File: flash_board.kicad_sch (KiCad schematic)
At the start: 9 parts, among them J1 Conn_02x16_Row_Letter_First, J2 Conn_02x03_Counter_Clockwise, U1 SST39SF040

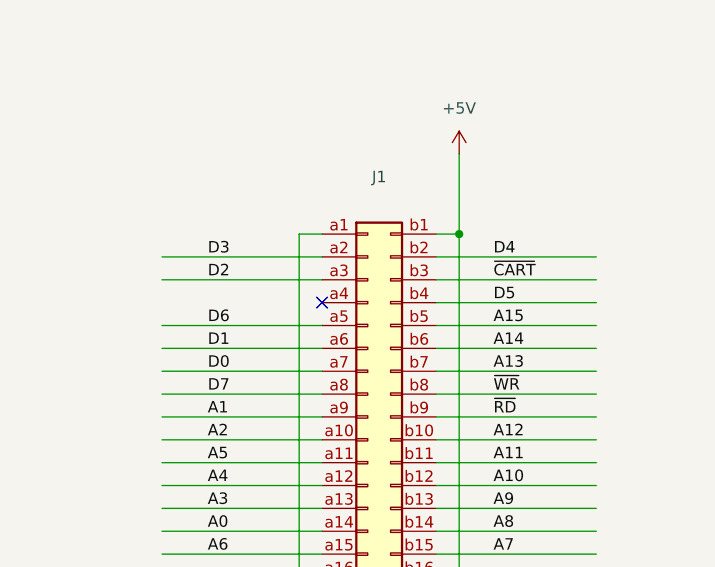
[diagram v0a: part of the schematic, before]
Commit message: Fixed D5 location on connector.
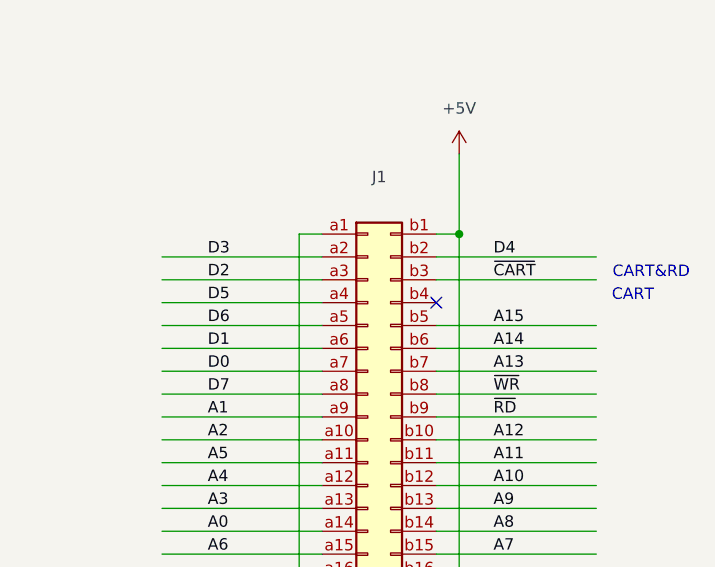
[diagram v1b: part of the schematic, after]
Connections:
- net D5: now also J1.a4 (Pin_a4); no longer J1.b4 (Pin_b4)
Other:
- note added: "CART"
- note added: "CART&RD"
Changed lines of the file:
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@@
 	)
 	(no_connect
-		(at 240.03 76.2)
+		(at 252.73 76.2)
 	)
 	(wire
@@
 	(wire
 		(pts
-			(xy 252.73 76.2) (xy 270.51 76.2)
+			(xy 222.25 76.2) (xy 240.03 76.2)
 		)
 		(stroke
@@
 			(width 0)
 			(type default)
+		)
+	)
+	(text "CART"
+		(exclude_from_sim no)
+		(at 274.574 75.438 0)
+		(effects
+			(font
+				(size 1.27 1.27)
+			)
+		)
+	)
+	(text "CART&RD"
+		(exclude_from_sim no)
+		(at 276.606 72.898 0)
+		(effects
+			(font
+				(size 1.27 1.27)
+			)
 		)
 	)
@@
 	)
 	(label "D5"
-		(at 259.08 76.2 0)
-		(effects
-			(font
+		(at 227.33 76.2 0)
+		(effects
+			(font
